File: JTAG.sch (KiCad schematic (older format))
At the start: 39 parts, among them CN5 CONN_RCPT_USB2.0_MINI_B_SMD_R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, U15 FT2232HL-REEL, X2 ABM3B-12.000MHZ

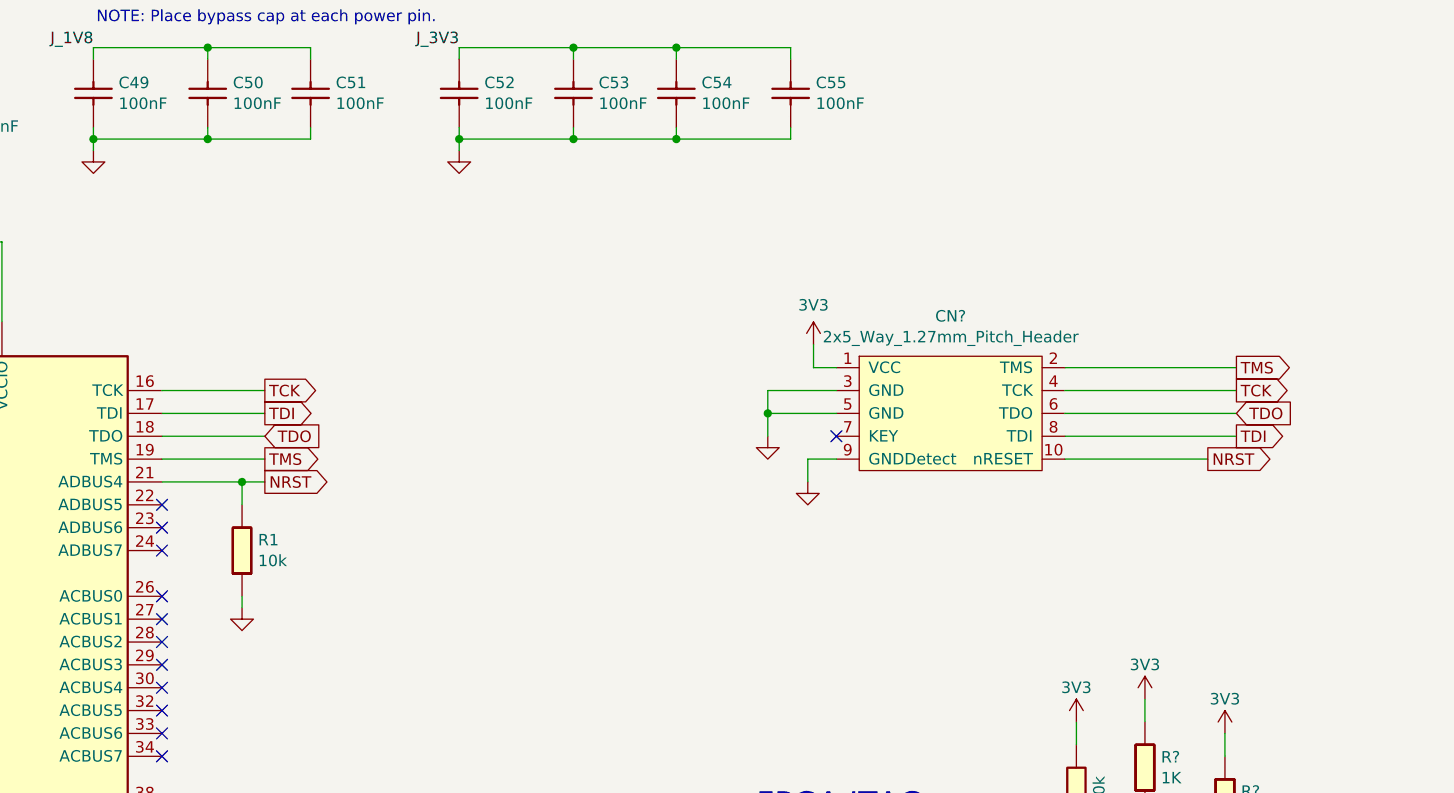
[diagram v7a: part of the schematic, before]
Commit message: JTAG Header has been added to the FTDI chip output
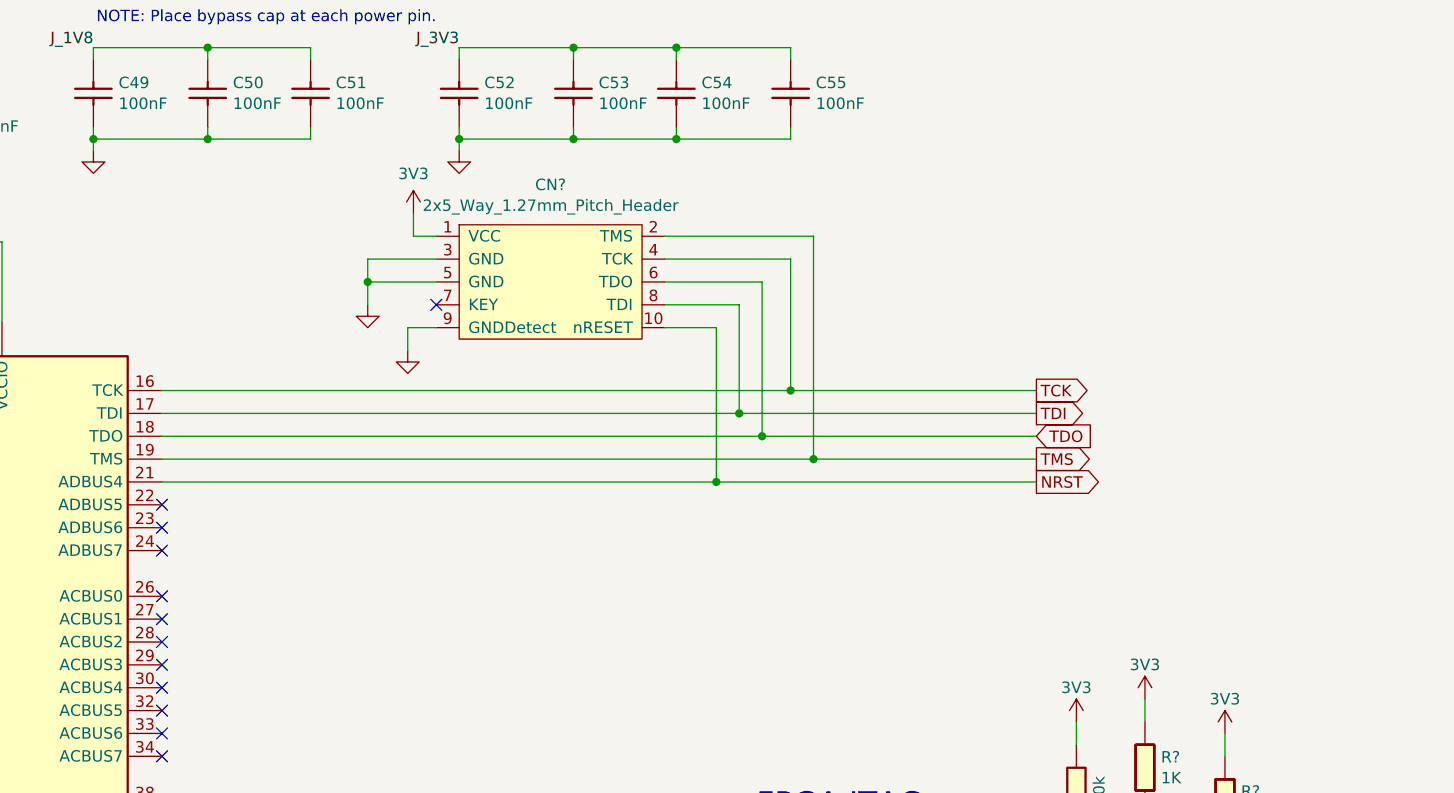
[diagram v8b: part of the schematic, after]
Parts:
- removed R1: 10k_0603_Chip_Resistor,_1%,_0.1W, symbol OpenVent:10k_0603_Chip_Resistor,_1%,_0.1W
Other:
- moved on the sheet: CN?
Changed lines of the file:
@@
 Wire Wire Line
 	2450 5350 2450 5400
-Text GLabel 5950 2550 2    50   Output ~ 0
+Text GLabel 9325 2550 2    50   Output ~ 0
 TCK
-Text GLabel 5950 2650 2    50   Output ~ 0
+Text GLabel 9325 2650 2    50   Output ~ 0
 TDI
-Text GLabel 5950 2750 2    50   Input ~ 0
+Text GLabel 9325 2750 2    50   Input ~ 0
 TDO
-Text GLabel 5950 2850 2    50   Output ~ 0
+Text GLabel 9325 2850 2    50   Output ~ 0
 TMS
-Wire Wire Line
-	5500 2550 5950 2550
-Wire Wire Line
-	5950 2650 5500 2650
-Wire Wire Line
-	5500 2750 5950 2750
-Wire Wire Line
-	5950 2850 5500 2850
 NoConn ~ 1350 3750
 NoConn ~ 2500 3100
@@
 L OpenVent:GND #PWR02
 U 1 1 603ABA41
-P 8150 2750
-F 0 "#PWR02" H 8150 2500 50  0001 C CNN
-F 1 "GND" H 8150 2600 50  0001 C CNN
-F 2 "" H 8150 2750 50  0001 C CNN
-F 3 "" H 8150 2750 50  0001 C CNN
-	1    8150 2750
-	1    0    0    -1
-$EndComp
-Wire Wire Line
-	8450 2650 8150 2650
-Wire Wire Line
-	8150 2650 8150 2750
-Wire Wire Line
-	8450 2550 8150 2550
-Wire Wire Line
-	8150 2550 8150 2650
-Connection ~ 8150 2650
+P 6400 2175
+F 0 "#PWR02" H 6400 1925 50  0001 C CNN
+F 1 "GND" H 6400 2025 50  0001 C CNN
+F 2 "" H 6400 2175 50  0001 C CNN
+F 3 "" H 6400 2175 50  0001 C CNN
+	1    6400 2175
+	1    0    0    -1
+$EndComp
+Wire Wire Line
+	6700 2075 6400 2075
+Wire Wire Line
+	6400 2075 6400 2175
+Wire Wire Line
+	6700 1975 6400 1975
+Wire Wire Line
+	6400 1975 6400 2075
+Connection ~ 6400 2075
 $Comp
 L OpenVent:3V3 #PWR04
 U 1 1 603BA4C8
-P 8350 2350
-F 0 "#PWR04" H 8350 2200 50  0001 C CNN
-F 1 "3V3" H 8350 2523 50  0000 C CNN
-F 2 "" H 8350 2350 50  0001 C CNN
-F 3 "" H 8350 2350 50  0001 C CNN
-	1    8350 2350
-	1    0    0    -1
-$EndComp
-Wire Wire Line
-	8350 2350 8350 2450
-Wire Wire Line
-	8350 2450 8450 2450
-Text GLabel 10200 2550 2    50   Output ~ 0
-TCK
-Wire Wire Line
-	9450 2550 10200 2550
-Text GLabel 10200 2750 2    50   Output ~ 0
-TDI
-Text GLabel 10200 2650 2    50   Input ~ 0
-TDO
-Text GLabel 10200 2450 2    50   Output ~ 0
-TMS
-Wire Wire Line
-	10200 2750 9450 2750
-Wire Wire Line
-	9450 2650 10200 2650
-Wire Wire Line
-	10200 2450 9450 2450
-Text GLabel 10075 2850 2    50   Output ~ 0
-NRST
-Wire Wire Line
-	9450 2850 10075 2850
+P 6600 1775
+F 0 "#PWR04" H 6600 1625 50  0001 C CNN
+F 1 "3V3" H 6600 1948 50  0000 C CNN
+F 2 "" H 6600 1775 50  0001 C CNN
+F 3 "" H 6600 1775 50  0001 C CNN
+	1    6600 1775
+	1    0    0    -1
+$EndComp
+Wire Wire Line
+	6600 1775 6600 1875
+Wire Wire Line
+	6600 1875 6700 1875
+Wire Wire Line
+	7700 1975 8250 1975
+Wire Wire Line
+	7700 2075 8125 2075
+Wire Wire Line
+	7700 2275 7925 2275
 $Comp
 L OpenVent:GND #PWR03
 U 1 1 6041AEF9
-P 8325 2950
-F 0 "#PWR03" H 8325 2700 50  0001 C CNN
-F 1 "GND" H 8325 2800 50  0001 C CNN
-F 2 "" H 8325 2950 50  0001 C CNN
-F 3 "" H 8325 2950 50  0001 C CNN
-	1    8325 2950
-	1    0    0    -1
-$EndComp
-Wire Wire Line
-	8325 2850 8325 2950
-Wire Wire Line
-	8325 2850 8450 2850
-NoConn ~ 8450 2750
-Text GLabel 5950 2950 2    50   Output ~ 0
+P 6575 2375
+F 0 "#PWR03" H 6575 2125 50  0001 C CNN
+F 1 "GND" H 6575 2225 50  0001 C CNN
+F 2 "" H 6575 2375 50  0001 C CNN
+F 3 "" H 6575 2375 50  0001 C CNN
+	1    6575 2375
+	1    0    0    -1
+$EndComp
+Wire Wire Line
+	6575 2275 6575 2375
+Wire Wire Line
+	6575 2275 6700 2275
+NoConn ~ 6700 2175
+Text GLabel 9325 2950 2    50   Output ~ 0
 NRST
-$Comp
-L OpenVent:10k_0603_Chip_Resistor,_1%,_0.1W R1
-U 1 1 6053B2C9
-P 5950 3150
-F 0 "R1" V 6004 3120 50  0000 L CNN
-F 1 "10k_0603_Chip_Resistor,_1%,_0.1W" H 5950 3150 50  0001 C CNN
-F 2 "" H 5950 3150 50  0001 C CNN
-F 3 "" H 5950 3150 50  0001 C CNN
-F 4 "10k" V 6095 3120 50  0000 L CNN "Val"
-F 5 "1%" H 5950 3150 50  0001 C CNN "Tolerance"
-F 6 "0.1W" H 5950 3150 50  0001 C CNN "Watt"
-	1    5950 3150
-	0    1    1    0
-$EndComp
-$Comp
-L OpenVent:GND #PWR01
-U 1 1 6053CC72
-P 5850 3500
-F 0 "#PWR01" H 5850 3250 50  0001 C CNN
-F 1 "GND" H 5850 3350 50  0001 C CNN
-F 2 "" H 5850 3500 50  0001 C CNN
-F 3 "" H 5850 3500 50  0001 C CNN
-	1    5850 3500
-	1    0    0    -1
-$EndComp
-Wire Wire Line
-	5850 3450 5850 3500
-Wire Wire Line
-	5500 2950 5850 2950
-Wire Wire Line
-	5850 3050 5850 2950
-Connection ~ 5850 2950
-Wire Wire Line
-	5850 2950 5950 2950
 $Comp
 L OpenVent:2x5_Way_1.27mm_Pitch_Header CN?
 U 1 1 6053C246
-P 8950 2300
-F 0 "CN?" H 8950 2375 50  0000 C CNN
-F 1 "2x5_Way_1.27mm_Pitch_Header" H 8950 2284 50  0000 C CNN
-F 2 "" H 8950 2300 50  0001 C CNN
-F 3 "http://www.cnctech.us/idcmatching2.pdf" H 8950 2300 50  0001 C CNN
-	1    8950 2300
+P 7200 1725
+F 0 "CN?" H 7200 1800 50  0000 C CNN
+F 1 "2x5_Way_1.27mm_Pitch_Header" H 7200 1709 50  0000 C CNN
+F 2 "" H 7200 1725 50  0001 C CNN
+F 3 "http://www.cnctech.us/idcmatching2.pdf" H 7200 1725 50  0001 C CNN
+	1    7200 1725
 	1    0    0    -1
 $EndComp
@@
 Wire Wire Line
 	750  4150 750  4200
+Wire Wire Line
+	5500 2550 8250 2550
+Wire Wire Line
+	5500 2650 8025 2650
+Wire Wire Line
+	5500 2750 8125 2750
+Wire Wire Line
+	5500 2850 8350 2850
+Wire Wire Line
+	5500 2950 7925 2950
+Wire Wire Line
+	7925 2275 7925 2950
+Connection ~ 7925 2950
+Wire Wire Line
+	7925 2950 9325 2950
+Wire Wire Line
+	8025 2175 8025 2650
+Wire Wire Line
+	8025 2175 7700 2175
+Connection ~ 8025 2650
+Wire Wire Line
+	8025 2650 9325 2650
+Wire Wire Line
+	8125 2075 8125 2750
+Connection ~ 8125 2750
+Wire Wire Line
+	8125 2750 9325 2750
+Wire Wire Line
+	8250 1975 8250 2550
+Connection ~ 8250 2550
+Wire Wire Line
+	8250 2550 9325 2550
+Connection ~ 8350 2850
+Wire Wire Line
+	8350 2850 9325 2850
+Wire Wire Line
+	8350 1875 8350 2850
+Wire Wire Line
+	8350 1875 7700 1875
 $EndSCHEMATC
